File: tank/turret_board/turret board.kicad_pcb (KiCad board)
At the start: 2 copper layers, 43.2 x 32.4 mm, 23 parts, among them J3 Conn_01x02_Male, Q1 2N3904, Q2 2N3904, U1 KA378R33, U2 pixart_ir, Y1 Crystal_4pin

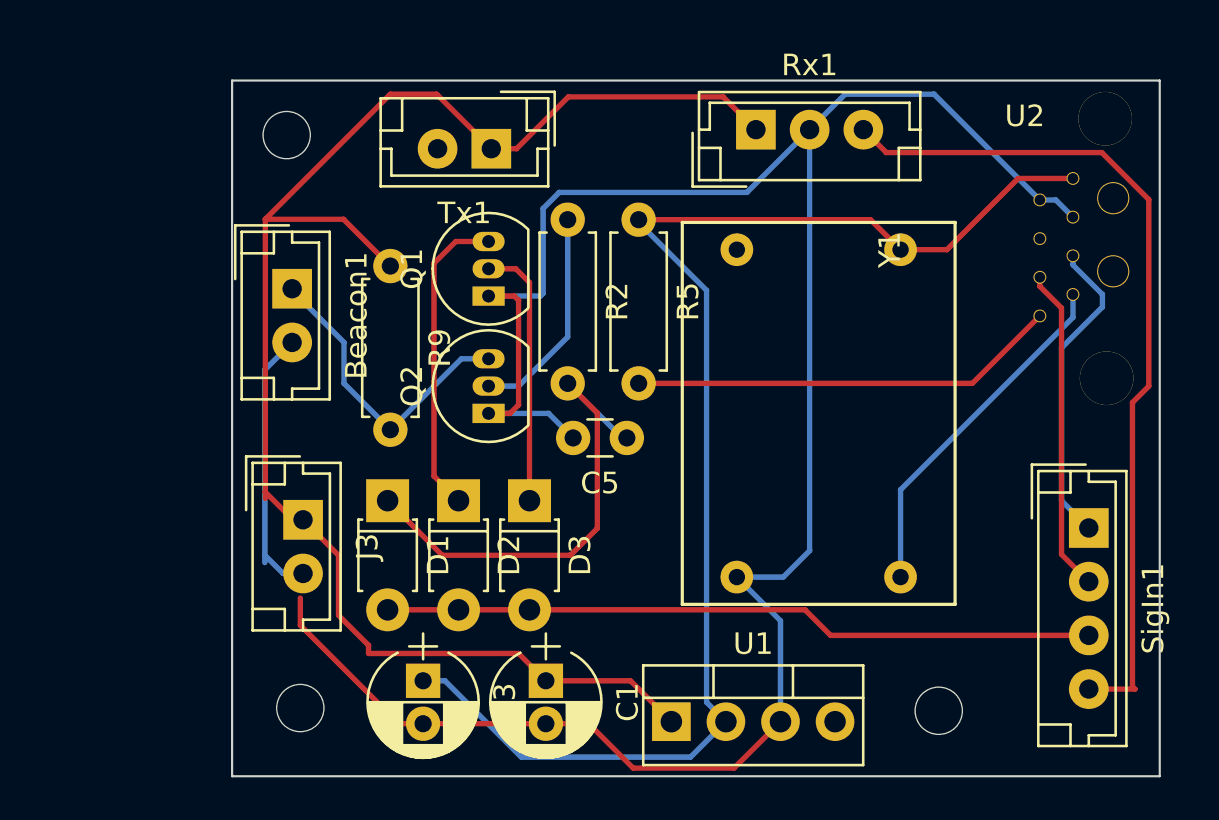
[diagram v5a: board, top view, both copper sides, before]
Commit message: Turret Board Version 0.6: - change camera orientation to better fit in turret - updated footprints
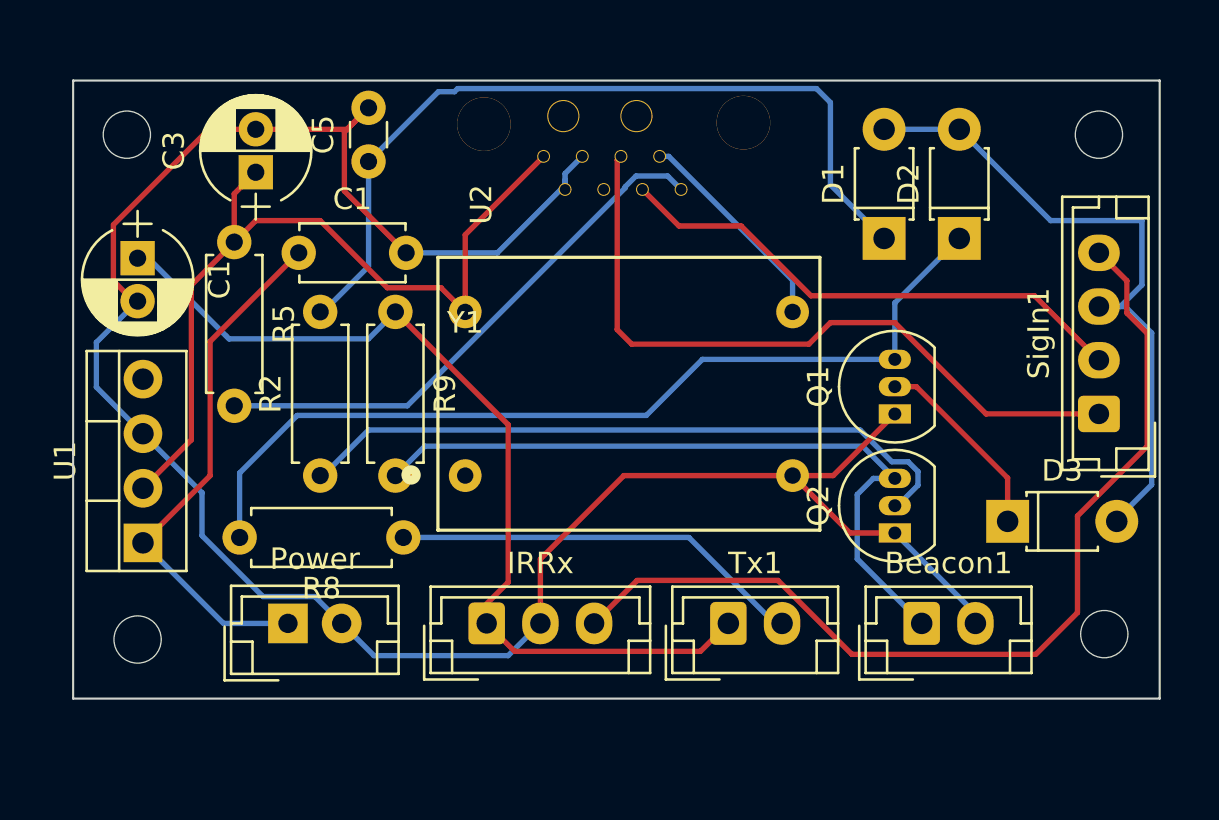
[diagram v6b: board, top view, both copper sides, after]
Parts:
- removed Rx1: CONN_01X03, JST:JST_EH_B03B-EH-A_03x2.50mm_Straight
- added C1: C_Small, Capacitor_THT:C_Disc_D4.7mm_W2.5mm_P5.00mm, F.Cu at (187.2, 102.0)
- added IRRx: CONN_01X03, Connector_JST:JST_EH_B3B-EH-A_1x03_P2.50mm_Vertical, F.Cu at (196.0, 119.2)
- added R8: R, Resistor_THT:R_Axial_DIN0207_L6.3mm_D2.5mm_P7.62mm_Horizontal, F.Cu at (192.1, 115.2)
- added REF**: MountingHole_2.2mm_M2, Mounting_Holes:MountingHole_2.2mm_M2, F.Cu at (224.5, 96.5)
- Beacon1, Tx1: footprint JST:JST_EH_B02B-EH-A_02x2.50mm_Straight -> Connector_JST:JST_EH_B2B-EH-A_1x02_P2.50mm_Vertical
- SigIn1: footprint JST:JST_EH_B04B-EH-A_04x2.50mm_Straight -> Connector_JST:JST_EH_B4B-EH-A_1x04_P2.50mm_Vertical
- moved Beacon1 33.2 mm to (216.2, 119.2), turned to 0 degrees
- moved C1 27.4 mm to (179.8, 102.2)
- moved D2 26.3 mm to (218.0, 101.3), turned to 90 degrees
- moved U2 26.2 mm to (195.2, 99.8), turned to 90 degrees
- moved D1 26.1 mm to (214.5, 101.3), turned to 90 degrees
- moved U1 26.0 mm to (180.0, 115.5), turned to 90 degrees
- moved C3 24.9 mm to (185.2, 98.2), turned to 90 degrees
- moved Tx1 24.7 mm to (207.2, 119.2), turned to 0 degrees
- moved D3 22.3 mm to (220.2, 114.5), turned to 0 degrees
- moved Y1 20.5 mm to (195.0, 104.8), turned to 0 degrees
- moved Q2 19.7 mm to (215.0, 115.0)
- moved Q1 19.7 mm to (215.0, 109.5)
- moved R5 18.9 mm to (184.2, 101.5)
- moved C5 17.6 mm to (190.5, 97.8), turned to 90 degrees
- moved R2 16.6 mm to (188.2, 112.4), turned to 90 degrees
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- renumbered J3 to Power
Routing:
- net 5V: track 72.8 -> 43.1 mm
- net Net-(D2-Pad1): track 14.5 -> 42.6 mm
- net 3.3V: track 63.7 -> 38.6 mm
- net Net-(C1-Pad1): track 0.00 -> 24.8 mm
- net Net-(Q2-Pad2): track 10.1 -> 31.7 mm
- net Beacon: track 14.4 -> 33.7 mm
- net IRTx: track 0.00 -> 19.3 mm
- net SLC: track 14.6 -> 33.0 mm
- net Net-(C5-Pad1): track 22.7 -> 38.6 mm
- net GND: track 119.3 -> 103.7 mm
- net SDA: track 15.1 -> 24.5 mm
- net Net-(U2-Pad7): track 16.5 -> 10.1 mm
- net RESET: track 20.1 -> 25.5 mm
- net IRRx: track 39.9 -> 44.6 mm
- net Net-(D3-Pad1): track 12.3 -> 9.03 mm
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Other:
- board size 43.2 x 32.4 mm -> 50.6 x 28.8 mm
- board text added: "Turret Board v0.6 Laser Tag Robot Tank M.I.A.R. Labs nick.groesz@gmail.com"
- board text removed: "Turret Board v0.5 Laser Tag Robot Tank M.I.A.R. Labs nick.groesz@gmail.com"

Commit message: and all that jazz
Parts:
- moved C5 30.2 mm to (212.5, 118.5)
- moved R2 26.9 mm to (213.8, 103.8), turned to 270 degrees
- moved Q1 23.5 mm to (191.5, 109.0), turned to 0 degrees
- moved D1 17.4 mm to (209.6, 118.0), turned to 180 degrees
- moved R5 16.5 mm to (194.4, 114.5), turned to 0 degrees
- moved D2 15.6 mm to (209.6, 114.5), turned to 180 degrees
- moved D3 14.7 mm to (214.0, 101.2), turned to 90 degrees
- moved Power 14.3 mm to (185.2, 105.0), turned to 90 degrees
- moved C1 12.8 mm to (192.5, 102.2)
- moved C1 10.1 mm to (197.2, 100.5), turned to 90 degrees
- moved Y1 9.37 mm to (201.8, 111.2), turned to 90 degrees
- moved C3 7.45 mm to (192.5, 96.4), turned to 270 degrees
- moved REF** 7.30 mm to (219.0, 124.2)
- moved U2 7.25 mm to (195.2, 92.5)
- moved SigIn1 6.54 mm to (218.0, 110.2)
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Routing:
- net Net-(C5-Pad1): track 38.6 -> 11.7 mm
- net Net-(D2-Pad1): track 42.6 -> 22.7 mm
- net Net-(D3-Pad1): track 9.03 -> 25.9 mm
- net Net-(Q2-Pad2): track 31.7 -> 14.8 mm
- net 5V: track 43.1 -> 53.7 mm
- net 3.3V: track 38.6 -> 46.3 mm
- net IRTx: track 19.3 -> 12.0 mm
- net Net-(C1-Pad1): track 24.8 -> 31.4 mm
- net SDA: track 24.5 -> 28.5 mm
- net GND: track 103.7 -> 99.8 mm
- net Net-(U2-Pad7): track 10.1 -> 6.70 mm
- net IRSig: track 31.6 -> 33.8 mm
- net Beacon: track 33.7 -> 31.6 mm
- net RESET: track 25.5 -> 24.0 mm
- net IRRx: track 44.6 -> 45.4 mm
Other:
- board size 50.6 x 28.8 mm -> 38 x 38.7 mm
- board text added: "Turret Board v0.7 Laser Tag Robot Tank M.I.A.R. Labs nick.groesz@gmail.com"
- board text removed: "Turret Board v0.6 Laser Tag Robot Tank M.I.A.R. Labs nick.groesz@gmail.com"
